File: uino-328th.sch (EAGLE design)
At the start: 11 parts, among them J1 USB_MICRO_B_2.0-TH

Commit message: Schematic complete.
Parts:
- removed ANALOG, POWER: (no value), SparkFun:M06SIP
- removed ICSP: M03X2, adilinden:M03X2
- removed IOH, IOL: (no value), SparkFun:M081X08
- removed U$1: ATMEGA328P-UINO2-P, adi-atmega:ATMEGA328P-UINO2-P
- removed U$2: PIC16F1454-P, adi-pic:PIC16F1454-P
- added C10, C2, C4, C5, C6, C7, C8, C9: (no value), rc-master-th:C_C025-040X018
- added C3: (no value), rc-master-th:CP_TT025-040
- added D2, D3, D4: (no value), SparkFun-LED:LED3MM
- added F1, F2: (no value), adi-misc:FUSE_PTC-1206
- added J2: USB_MICRO_B_2.0-TH, adi-misc:USB_MICRO_B_2.0-TH
- added J3: (no value), SparkFun-Connectors:M06LOCK
- added JP1, JP2: SJ-035, jumpers:SJ-035
- added JP3: M03X2, adi-misc:M03X2
- added JP4, JP5: (no value), SparkFun:M06SIP
- added JP6, JP7: (no value), SparkFun:M081X08
- added R2, R3, R4, R5, R6, R7: (no value), rc-master-th:R_038X018
- added T1: (no value), zetex:PMOSSOT223
- added U1: AP1117E, v-reg:AP1117E
- added U2: PIC16F1454-P, adi-pic:PIC16F1454-P
- added U3: ATMEGA328P-P, adi-atmega:ATMEGA328P-P
- added Y1: (no value), crystal:CRYTALHC49S
- C1: device rc-master-th:C_C025-040X018 -> rc-master-th:CP_TT025-040
- D1: value (none) -> 1N4004-7; device led:LED3MM -> diode:1N4004-7
- J1: value USB_MICRO_B_2.0-TH -> CON_TERMINAL_BLOCK_02-5MM; device adilinden:USB_MICRO_B_2.0-TH -> dp_devices.v6:CON_TERMINAL_BLOCK_02-5MM
- R1: device rc-master-th:R_X0204/7 -> rc-master-th:R_038X018
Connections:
- removed net VCC: ICSP.2
- new net CLKIN: C8.2, JP2.2, U3.PB6(PCINT6/XTAL1/TOSC1), Y1.2
- new net CLKOUT: JP2.1, U2.(CLKOUT)RA4
- new net DTR: JP1.1, U2.RC3
- new net ICSPCLK: J3.5, R4.1, U2.(ICSPCLK)RC1
- new net ICSPDAT: J3.4, R6.1, U2.(ICSPDAT)RC0
- new net LVP: J3.6
- new net N$10: R5.2, U2.(RX)RC5
- new net N$12: D2.C, R4.2
- new net N$13: D3.C, R6.2
- new net N$15: F2.2, T1.D, T1.D2
- new net N$5: D4.A, R7.1
- new net N$6: J2.ID
- new net N$7: C9.2, U3.PB7(PCINT7/XTAL2/TOSC2), Y1.1
- new net N$8: F1.1, J1.2
- new net N$9: R3.2, U2.(TX)RC4
- new net VPP: J3.1, R1.1, U2.RA3(MCLR/VPP)
- new net VUSB: F2.1, J2.VBUS
- net 3V3: now also JP4.2; no longer POWER.2
- net 5V: now also C3.+, C4.2, C5.2, C6.2, D2.A, D3.A, J3.2, JP3.2, JP4.3, R1.2, R2.2, T1.S, U1.OUT, U2.VDD, U3.AVCC, U3.VCC; no longer POWER.3
- net A0: now also JP5.1, U3.(ADC0/PCINT8)PC0; no longer ANALOG.1, U$1.(ADC0/PCINT8)PC0
- net A1: now also JP5.2, U3.(ADC1/PCINT9)PC1; no longer ANALOG.2, U$1.(ADC1/PCINT9)PC1
- net A2: now also JP5.3, U3.(ADC2/PCINT10)PC2; no longer ANALOG.3, U$1.(ADC2/PCINT10)PC2
- net A3: now also JP5.4, U3.(ADC3/PCINT11)PC3; no longer ANALOG.4, U$1.(ADC3/PCINT11)PC3
- net A4/SDA: now also JP5.5, U3.(ADC4/SDA/PCINT12)PC4; no longer ANALOG.5, U$1.(ADC4/SDA/PCINT12)PC4
- net A5/SCL: now also JP5.6, U3.(ADC5/SCL/PCINT13)PC5; no longer ANALOG.6, U$1.(ADC5/SCL/PCINT13)PC5
- net AREF: now also C10.2, JP7.8, U3.AREF; no longer C1.1, IOH.8, U$1.AREF
- net D0/RXD: now also JP6.1, R3.1, U3.(PCINT16/RXD)PD0; no longer IOL.1, U$1.(PCINT16/RXD)PD0
- net D1/TXD: now also JP6.2, R5.1, U3.(PCINT17/TXD)PD1; no longer IOL.2, U$1.(PCINT17/TXD)PD1
- net D10/SS: now also JP7.3, U3.(SS/OC1B/PCINT2)PB2; no longer IOH.3, U$1.(SS/OC1B/PCINT2)PB2
- net D11/MOSI: now also JP3.4, JP7.4, U3.(MOSI/OC2A/PCINT3)PB3; no longer ICSP.4, IOH.4, U$1.(MOSI/OC2A/PCINT3)PB3
- net D12/MISO: now also JP3.1, JP7.5, U3.(MISO/PCINT4)PB4; no longer ICSP.1, IOH.5, U$1.(MISO/PCINT4)PB4
- net D13/SCK: now also JP3.3, JP7.6, R7.2, U3.(SCK/PCINT5)PB5; no longer ICSP.3, IOH.6, R1.2, U$1.(SCK/PCINT5)PB5
- net D2: now also JP6.3, U3.(PCINT18/INT0)PD2; no longer IOL.3, U$1.(PCINT18/INT0)PD2
- net D3: now also JP6.4, U3.(PCINT19/OC2B/INT1)PD3; no longer IOL.4, U$1.(PCINT19/OC2B/INT1)PD3
- net D4: now also JP6.5, U3.(PCINT20/XCK/T0)PD4; no longer IOL.5, U$1.(PCINT20/XCK/T0)PD4
- net D5: now also JP6.6, U3.(PCINT21/OC0B/T1)PD5; no longer IOL.6, U$1.(PCINT21/OC0B/T1)PD5
- net D6: now also JP6.7, U3.(PCINT22/OC0A/AIN0)PD6; no longer IOL.7, U$1.(PCINT22/OC0A/AIN0)PD6
- net D7: now also JP6.8, U3.(PCINT23/AIN1)PD7; no longer IOL.8, U$1.(PCINT23/AIN1)PD7
- net D8: now also JP7.1, U3.(PCINT0/CLKO/ICP1)PB0; no longer IOH.1, U$1.(PCINT0/CLKO/ICP1)PB0
- net D9: now also JP7.2, U3.(OC1A/PCINT1)PB1; no longer IOH.2, U$1.(OC1A/PCINT1)PB1
- net GND: now also C1.-, C10.1, C2.1, C3.-, C4.1, C5.1, C6.1, C8.1, C9.1, D1.A, D4.C, J1.1, J2.GND, J2.S1, J2.S2, J3.3, JP3.6, JP4.4, JP4.5, JP7.7, T1.G, U1.GND, U2.VSS, U3.AGND, U3.GND; no longer C1.2, D1.C, ICSP.6, IOH.7, POWER.4, POWER.5
- net N$1: now also C2.2, U2.VUSB3V3; no longer J1.D-, U$2.RA1(D-)
- net N$2: now also C7.1, JP1.2; no longer J1.D+, U$2.RA0(D+)
- net N$3: now also J2.D-, U2.RA1(D-); no longer J1.GND, J1.S1
- net N$4: now also J2.D+, U2.RA0(D+); no longer D1.A, R1.1
- net RESET: now also C7.2, JP3.5, JP4.1, R2.1, U3.PC6(PCINT14/RESET); no longer ICSP.5, POWER.1
- net VIN: now also C1.+, D1.C, F1.2, JP4.6, U1.IN; no longer POWER.6
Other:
- note added: "*uino-328th"
- note added: "v0.1 2016/10/25 by Adi Linden for Mathew"
- moved on the sheet: R1

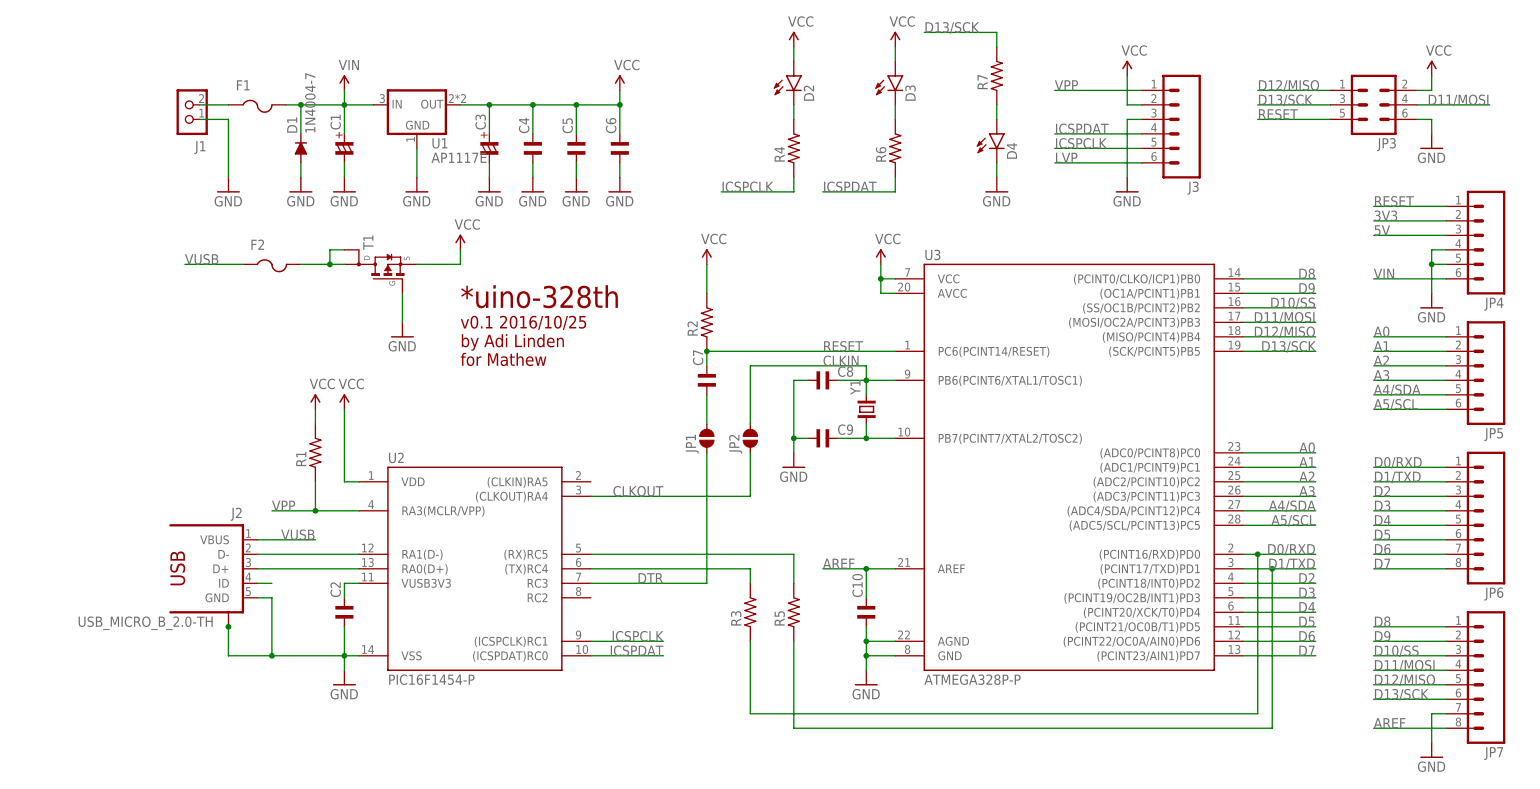
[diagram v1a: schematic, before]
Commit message: Changed to 3V3 and 5V hybrid.
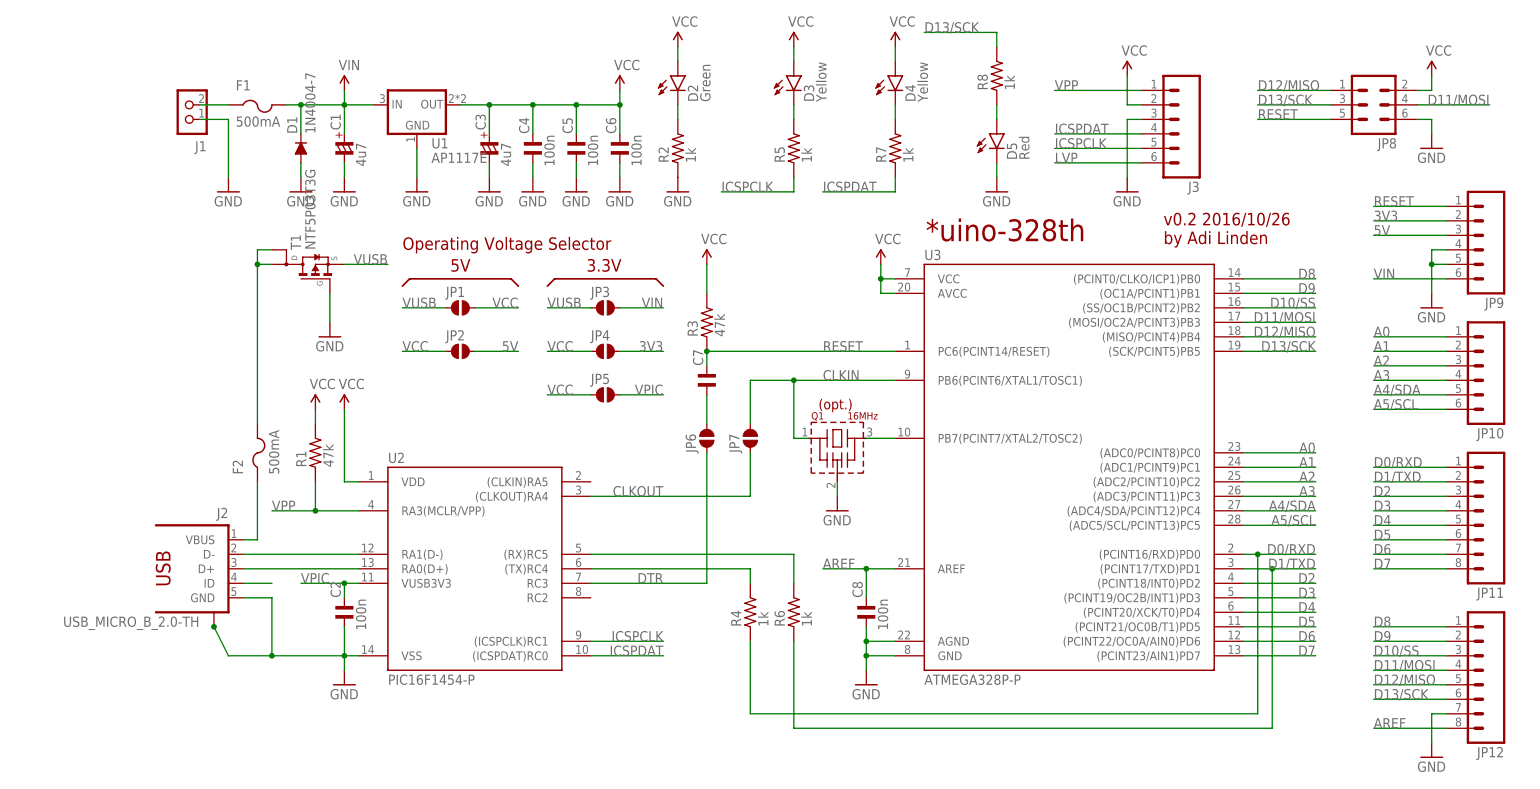
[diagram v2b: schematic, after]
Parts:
- removed C10, C9: (no value), rc-master-th:C_C025-040X018
- removed Y1: (no value), crystal:CRYTALHC49S
- added D5: Red, SparkFun-LED:LED3MM
- added JP10, JP9: (no value), SparkFun:M06SIP
- added JP11, JP12: (no value), SparkFun:M081X08
- added JP8: M03X2, adi-misc:M03X2
- added Q1: 16MHz, murata-resonators:CSTLS_X
- added R8: 1k, rc-master-th:R_038X018
- C1, C3: value (none) -> 4u7
- C2, C4, C5, C6, C8: value (none) -> 100n
- D2: value (none) -> Green
- D3, D4: value (none) -> Yellow
- F1, F2: value (none) -> 500mA
- JP3: value M03X2 -> SJ-035; device adi-misc:M03X2 -> jumpers:SJ-035
- JP4, JP5: value (none) -> SJ-035; device SparkFun:M06SIP -> jumpers:SJ-035
- JP6, JP7: value (none) -> SJ-035; device SparkFun:M081X08 -> jumpers:SJ-035
- R1, R3: value (none) -> 47k
- R2, R4, R5, R6, R7: value (none) -> 1k
- T1: value (none) -> NTF5P03T3G
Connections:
- new net N$11: Q1.3, U3.PB7(PCINT7/XTAL2/TOSC2)
- new net VCC: C3.+, C4.2, C5.2, C6.2, D2.A, D3.A, D4.A, J3.2, JP1.2, JP2.1, JP4.1, JP5.1, JP8.2, R1.2, R3.2, U1.OUT, U2.VDD, U3.AVCC, U3.VCC
- new net VPIC: C2.2, JP5.2, U2.VUSB3V3
- net 3V3: now also JP9.2
- net 5V: now also JP2.2, JP9.3; no longer C3.+, C4.2, C5.2, C6.2, D2.A, D3.A, J3.2, JP3.2, JP4.3, R1.2, R2.2, T1.S, U1.OUT, U2.VDD, U3.AVCC, U3.VCC
- net A0: now also JP10.1; no longer JP5.1
- net A1: now also JP10.2; no longer JP5.2
- net A2: now also JP10.3; no longer JP5.3
- net A3: now also JP10.4; no longer JP5.4
- net A4/SDA: now also JP10.5; no longer JP5.5
- net A5/SCL: now also JP10.6; no longer JP5.6
- net AREF: now also C8.2, JP12.8; no longer C10.2, JP7.8
- net CLKIN: now also JP7.2, Q1.1; no longer C8.2, JP2.2, Y1.2
- net CLKOUT: now also JP7.1; no longer JP2.1
- net D0/RXD: now also JP11.1, R4.1; no longer JP6.1, R3.1
- net D1/TXD: now also JP11.2, R6.1; no longer JP6.2, R5.1
- net D10/SS: now also JP12.3; no longer JP7.3
- net D11/MOSI: now also JP12.4, JP8.4; no longer JP3.4, JP7.4
- net D12/MISO: now also JP12.5, JP8.1; no longer JP3.1, JP7.5
- net D13/SCK: now also JP12.6, JP8.3, R8.2; no longer JP3.3, JP7.6, R7.2
- net D2: now also JP11.3; no longer JP6.3
- net D3: now also JP11.4; no longer JP6.4
- net D4: now also JP11.5; no longer JP6.5
- net D5: now also JP11.6; no longer JP6.6
- net D6: now also JP11.7; no longer JP6.7
- net D7: now also JP11.8; no longer JP6.8
- net D8: now also JP12.1; no longer JP7.1
- net D9: now also JP12.2; no longer JP7.2
- net DTR: now also JP6.1; no longer JP1.1
- net GND: now also D5.C, JP12.7, JP8.6, JP9.4, JP9.5, Q1.VSS, R2.1; no longer C10.1, C9.1, D4.C, JP3.6, JP4.4, JP4.5, JP7.7
- net ICSPCLK: now also R5.1; no longer R4.1
- net ICSPDAT: now also R7.1; no longer R6.1
- net N$1: now also D2.C, R2.2; no longer C2.2, U2.VUSB3V3
- net N$10: now also R6.2; no longer R5.2
- net N$12: now also D3.C, R5.2; no longer D2.C, R4.2
- net N$13: now also D4.C, R7.2; no longer D3.C, R6.2
- net N$2: now also JP6.2; no longer JP1.2
- net N$5: now also D5.A, R8.1; no longer D4.A, R7.1
- net N$7: now also F2.1, J2.VBUS; no longer C9.2, U3.PB7(PCINT7/XTAL2/TOSC2), Y1.1
- net N$9: now also R4.2; no longer R3.2
- net RESET: now also JP8.5, JP9.1, R3.1; no longer JP3.5, JP4.1, R2.1
- net VIN: now also JP3.2, JP9.6; no longer JP4.6
- net VUSB: now also JP1.1, JP3.1, T1.S; no longer F2.1, J2.VBUS
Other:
- note added: "(opt.)"
- note added: "3.3V"
- note added: "5V"
- note added: "Operating Voltage Selector"
- note added: "v0.2 2016/10/26 by Adi Linden"
- note removed: "v0.1 2016/10/25 by Adi Linden for Mathew"
- moved on the sheet: C8, D2, D3, D4, F2, J2, JP1, JP2, R2, R3, R4, R5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

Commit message: Attempts at routing board.
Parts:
- R1, R2, R3, R5, R7: device rc-master-th:R_038X018 -> rc-master:R_X0207/7
- R4, R6, R8: device rc-master-th:R_038X018 -> rc-master:R_X0207/10
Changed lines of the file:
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@@
 <setting verticaltext="up"/>
 </settings>
-<grid distance="0.1" unitdist="inch" unit="inch" style="lines" multiple="1" display="yes" altdistance="0.01" altunitdist="inch" altunit="inch"/>
+<grid distance="0.1" unitdist="inch" unit="inch" style="lines" multiple="1" display="no" altdistance="0.01" altunitdist="inch" altunit="inch"/>
 <layers>
 <layer number="1" name="Top" color="4" fill="1" visible="no" active="no"/>
@@
 <layer number="18" name="Vias" color="2" fill="1" visible="no" active="no"/>
 <layer number="19" name="Unrouted" color="6" fill="1" visible="no" active="no"/>
-<layer number="20" name="Dimension" color="7" fill="1" visible="no" active="no"/>
-<layer number="21" name="tPlace" color="16" fill="1" visible="no" active="no"/>
-<layer number="22" name="bPlace" color="14" fill="1" visible="no" active="no"/>
+<layer number="20" name="Dimension" color="15" fill="1" visible="no" active="no"/>
+<layer number="21" name="tPlace" color="7" fill="1" visible="no" active="no"/>
+<layer number="22" name="bPlace" color="7" fill="1" visible="no" active="no"/>
 <layer number="23" name="tOrigins" color="15" fill="1" visible="no" active="no"/>
 <layer number="24" name="bOrigins" color="15" fill="1" visible="no" active="no"/>
@@
 <layer number="29" name="tStop" color="7" fill="3" visible="no" active="no"/>
 <layer number="30" name="bStop" color="7" fill="6" visible="no" active="no"/>
-<layer number="31" name="tCream" color="11" fill="4" visible="no" active="no"/>
+<layer number="31" name="tCream" color="7" fill="4" visible="no" active="no"/>
 <layer number="32" name="bCream" color="7" fill="5" visible="no" active="no"/>
 <layer number="33" name="tFinish" color="6" fill="3" visible="no" active="no"/>
@@
 <layer number="47" name="Measures" color="7" fill="1" visible="no" active="no"/>
 <layer number="48" name="Document" color="7" fill="1" visible="no" active="no"/>
-<layer number="49" name="Reference" color="13" fill="1" visible="no" active="no"/>
-<layer number="50" name="dxf" color="7" fill="1" visible="no" active="no"/>
-<layer number="51" name="tDocu" color="14" fill="1" visible="no" active="no"/>
+<layer number="49" name="Reference" color="7" fill="1" visible="no" active="no"/>
+<layer number="50" name="dxf" color="12" fill="1" visible="no" active="no"/>
+<layer number="51" name="tDocu" color="7" fill="1" visible="no" active="no"/>
 <layer number="52" name="bDocu" color="7" fill="1" visible="no" active="no"/>
-<layer number="53" name="tGND_GNDA" color="7" fill="9" visible="no" active="no"/>
-<layer number="54" name="bGND_GNDA" color="1" fill="9" visible="no" active="no"/>
+<layer number="53" name="tGND_GNDA" color="7" fill="1" visible="no" active="no"/>
+<layer number="54" name="bGND_GNDA" color="7" fill="1" visible="no" active="no"/>
 <layer number="56" name="wert" color="7" fill="1" visible="no" active="no"/>
 <layer number="57" name="tCAD" color="7" fill="1" visible="no" active="no"/>
@@
 <part name="GND16" library="supply1" deviceset="GND" device=""/>
 <part name="SUPPLY11" library="SparkFun-Aesthetics" deviceset="VCC" device=""/>
-<part name="R4" library="rc-master-th" deviceset="R_" device="038X018" value="1k"/>
-<part name="R6" library="rc-master-th" deviceset="R_" device="038X018" value="1k"/>
+<part name="R4" library="rc-master" deviceset="R_" device="X0207/10" value="1k"/>
+<part name="R6" library="rc-master" deviceset="R_" device="X0207/10" value="1k"/>
 <part name="GND13" library="supply1" deviceset="GND" device=""/>
-<part name="R1" library="rc-master-th" deviceset="R_" device="038X018" value="47k"/>
+<part name="R1" library="rc-master" deviceset="R_" device="X0207/7" value="47k"/>
 <part name="C3" library="rc-master-th" deviceset="CP_" device="TT025-040" value="4u7"/>
 <part name="C1" library="rc-master-th" deviceset="CP_" device="TT025-040" value="4u7"/>
@@
 <part name="C8" library="rc-master-th" deviceset="C_" device="C025-040X018" value="100n"/>
 <part name="GND12" library="supply1" deviceset="GND" device=""/>
-<part name="R8" library="rc-master-th" deviceset="R_" device="038X018" value="1k"/>
+<part name="R8" library="rc-master" deviceset="R_" device="X0207/10" value="1k"/>
 <part name="SUPPLY3" library="SparkFun-Aesthetics" deviceset="VCC" device=""/>
 <part name="GND5" library="supply1" deviceset="GND" device=""/>
 <part name="C2" library="rc-master-th" deviceset="C_" device="C025-040X018" value="100n"/>
-<part name="R3" library="rc-master-th" deviceset="R_" device="038X018" value="47k"/>
+<part name="R3" library="rc-master" deviceset="R_" device="X0207/7" value="47k"/>
 <part name="J3" library="SparkFun-Connectors" deviceset="M06" device="LOCK"/>
 <part name="SUPPLY10" library="SparkFun-Aesthetics" deviceset="VCC" device=""/>
@@
 <part name="D4" library="SparkFun-LED" deviceset="LED" device="3MM" value="Yellow"/>
 <part name="D3" library="SparkFun-LED" deviceset="LED" device="3MM" value="Yellow"/>
-<part name="R5" library="rc-master-th" deviceset="R_" device="038X018" value="1k"/>
-<part name="R7" library="rc-master-th" deviceset="R_" device="038X018" value="1k"/>
+<part name="R5" library="rc-master" deviceset="R_" device="X0207/7" value="1k"/>
+<part name="R7" library="rc-master" deviceset="R_" device="X0207/7" value="1k"/>
 <part name="SUPPLY9" library="SparkFun-Aesthetics" deviceset="VCC" device=""/>
 <part name="SUPPLY7" library="SparkFun-Aesthetics" deviceset="VCC" device=""/>
@@
 <part name="SUPPLY2" library="SparkFun-Aesthetics" deviceset="VIN" device=""/>
 <part name="D2" library="SparkFun-LED" deviceset="LED" device="3MM" value="Green"/>
-<part name="R2" library="rc-master-th" deviceset="R_" device="038X018" value="1k"/>
+<part name="R2" library="rc-master" deviceset="R_" device="X0207/7" value="1k"/>
 <part name="SUPPLY5" library="SparkFun-Aesthetics" deviceset="VCC" device=""/>
 <part name="GND11" library="supply1" deviceset="GND" device=""/>

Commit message: First cut to try gerber.
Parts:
- removed C6: 100n, rc-master-th:C_C025-040X018
- removed JP10, JP9: (no value), SparkFun:M06SIP
- removed JP11, JP12: (no value), SparkFun:M081X08
- removed JP8: M03X2, adi-misc:M03X2
- removed T1: NTF5P03T3G, zetex:PMOSSOT223
- added D6: Red, SparkFun-LED:LED3MM
- added S1: TL1100X, adi-misc:TL1100X
- D1: value 1N4004-7 -> (none); device diode:1N4004-7 -> diode:SCHOTTKY-DIODEDO35-7
- D2: value Green -> (none); device SparkFun-LED:LED3MM -> diode:SCHOTTKY-DIODEDO35-7
- D3: value Yellow -> Green
- D5: value Red -> Yellow
- F1, F2: device adi-misc:FUSE_PTC-1206 -> adi-misc:FUSE_PTC-TH
- J1: device dp_devices.v6:CON_TERMINAL_BLOCK_02-5MM -> adi-misc:CON_TERMINAL_BLOCK_02-5MM
- JP3: value SJ-035 -> M03X2; device jumpers:SJ-035 -> adi-misc:M03X2
- JP4, JP5: value SJ-035 -> (none); device jumpers:SJ-035 -> SparkFun:M06SIP
- JP6, JP7: value SJ-035 -> (none); device jumpers:SJ-035 -> SparkFun:M081X08
- Q1: value 16MHz -> (none)
- U1: value AP1117E -> V_REG_MCP170X; device v-reg:AP1117E -> adi-misc:V_REG_MCP170X
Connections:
- removed net 3V3: JP4.2, JP9.2
- removed net N$15: F2.2, T1.D, T1.D2
- removed net N$7: F2.1, J2.VBUS
- removed net VPIC: C2.2, JP5.2, U2.VUSB3V3
- removed net VUSB: JP1.1, JP3.1, T1.S
- new net N$14: D2.A, F1.2
- new net VBUS: F1.1, J2.VBUS
- net 5V: now also JP4.3; no longer JP2.2, JP9.3
- net A0: now also JP5.1; no longer JP10.1
- net A1: now also JP5.2; no longer JP10.2
- net A2: now also JP5.3; no longer JP10.3
- net A3: now also JP5.4; no longer JP10.4
- net A4/SDA: now also JP5.5; no longer JP10.5
- net A5/SCL: now also JP5.6; no longer JP10.6
- net AREF: now also JP7.8; no longer JP12.8
- net CLKIN: now also JP2.2; no longer JP7.2
- net CLKOUT: now also JP2.1; no longer JP7.1
- net D0/RXD: now also JP6.1; no longer JP11.1
- net D1/TXD: now also JP6.2; no longer JP11.2
- net D10/SS: now also JP7.3; no longer JP12.3
- net D11/MOSI: now also JP3.4, JP7.4; no longer JP12.4, JP8.4
- net D12/MISO: now also JP3.1, JP7.5; no longer JP12.5, JP8.1
- net D13/SCK: now also JP3.3, JP7.6; no longer JP12.6, JP8.3
- net D2: now also JP6.3; no longer JP11.3
- net D3: now also JP6.4; no longer JP11.4
- net D4: now also JP6.5; no longer JP11.5
- net D5: now also JP6.6; no longer JP11.6
- net D6: now also JP6.7; no longer JP11.7
- net D7: now also JP6.8; no longer JP11.8
- net D8: now also JP7.1; no longer JP12.1
- net D9: now also JP7.2; no longer JP12.2
- net DTR: now also JP1.1; no longer JP6.1
- net GND: now also D6.C, JP3.6, JP4.4, JP4.5, JP7.7, S1.P, S1.P1; no longer C6.1, D5.C, JP12.7, JP8.6, JP9.4, JP9.5, T1.G
- net N$1: now also D3.C; no longer D2.C
- net N$12: now also D4.C; no longer D3.C
- net N$13: now also D5.C; no longer D4.C
- net N$2: now also JP1.2; no longer JP6.2
- net N$5: now also D6.A; no longer D5.A
- net N$8: now also F2.1; no longer F1.1
- net RESET: now also JP3.5, JP4.1, S1.S, S1.S1; no longer JP8.5, JP9.1
- net VCC: now also C2.2, D5.A, JP3.2, JP4.2, U2.VUSB3V3; no longer C6.2, D2.A, JP1.2, JP2.1, JP4.1, JP5.1, JP8.2
- net VIN: now also D2.C, F2.2, JP4.6; no longer F1.2, JP3.2, JP9.6
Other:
- note added: "v0.3 2016/10/30 by Adi Linden"
- note removed: "3.3V"
- note removed: "5V"
- note removed: "Operating Voltage Selector"
- note removed: "v0.2 2016/10/26 by Adi Linden"
- moved on the sheet: C1, C3, C4, C5, C7, D3, D4, D5, F1, F2, J1, JP1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
